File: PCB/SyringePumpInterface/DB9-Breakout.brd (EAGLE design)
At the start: 37.3 x 32.5 mm, 3 parts, among them J2 AUDIO_JACK_3.5MM_PTH

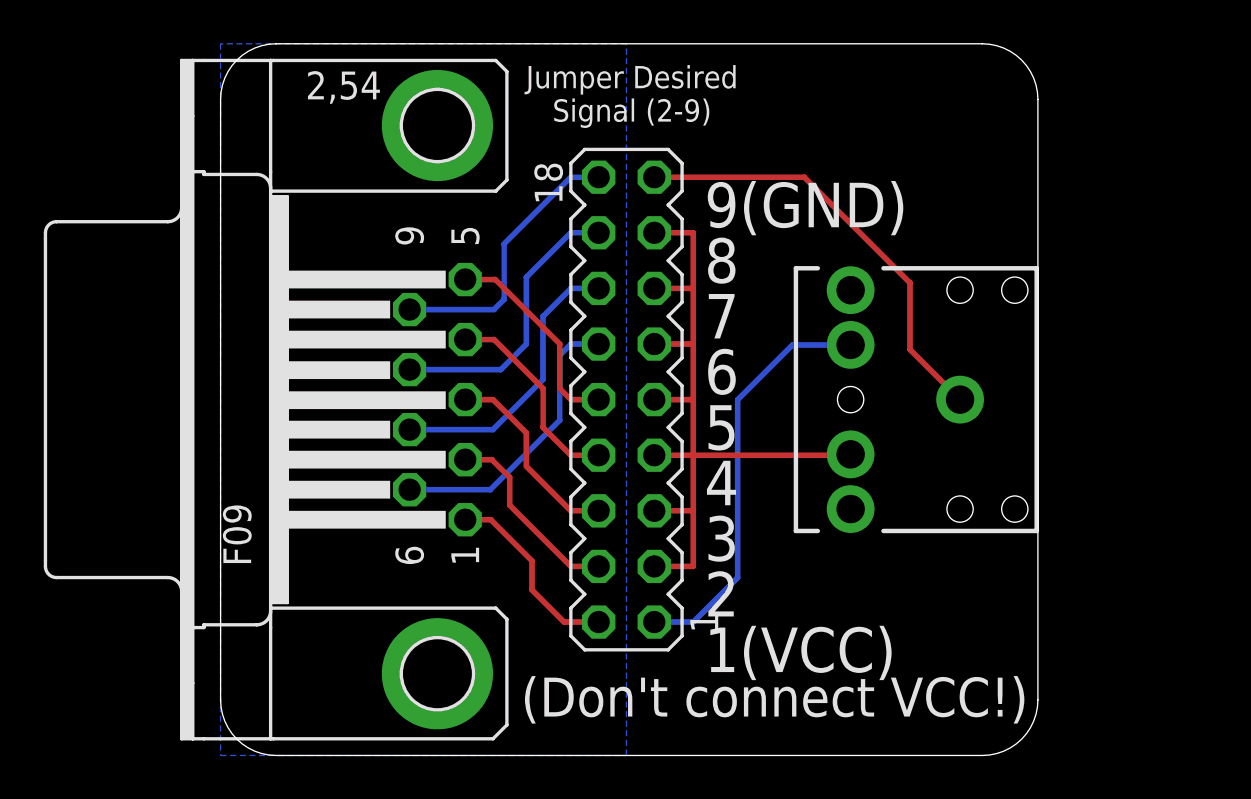
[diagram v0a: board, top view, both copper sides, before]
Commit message: New mouse-scale nose poke foodwell designs added. Also a flexible PCB beam break pcb. Also updated DB9 breakout for the syringe pump that has a jumper to choose the pulse pin.
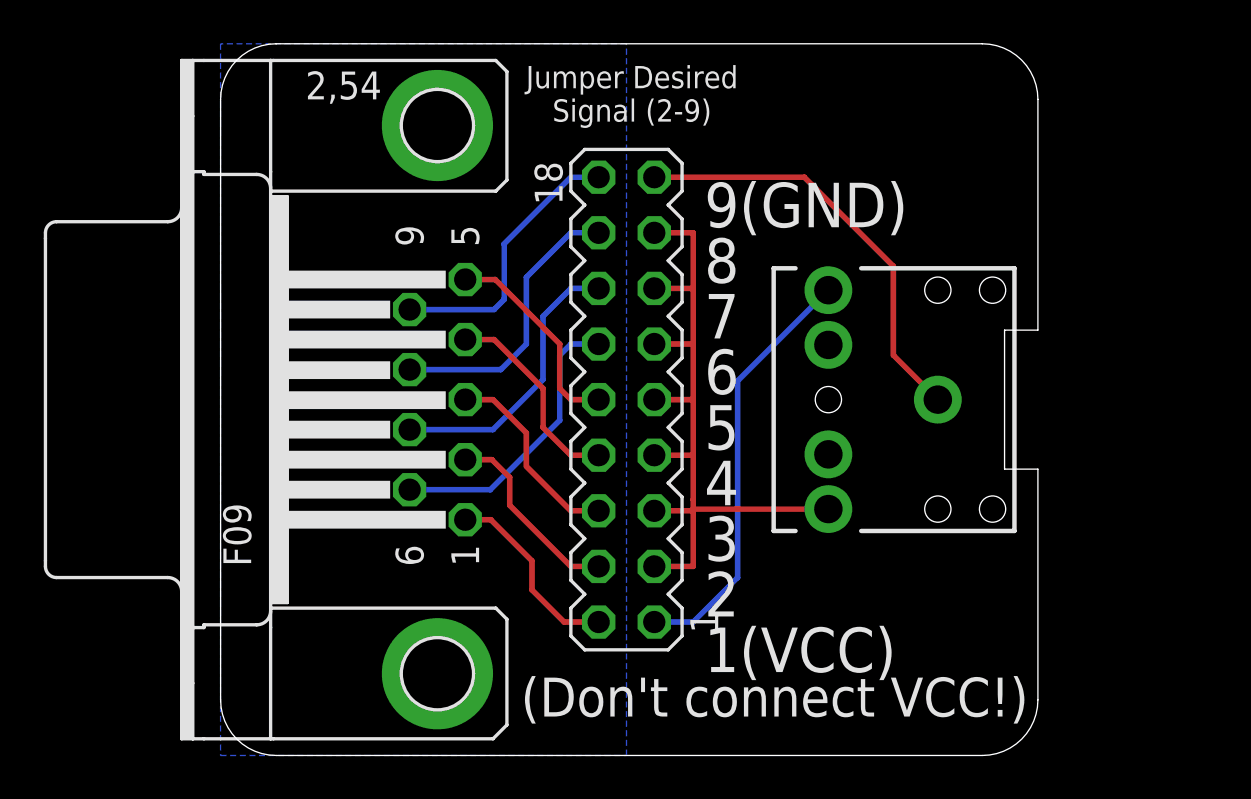
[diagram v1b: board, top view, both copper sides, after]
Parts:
- moved J2 1.02 mm to (32.8, 16.3)
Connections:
- net SIGNAL: now also J2.RING; no longer J2.RSH
- net VCC: now also J2.TIP; no longer J2.TSH
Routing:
- net SIGNAL: track 34.9 -> 33.9 mm
- net VCC: track 19.0 -> 19.5 mm
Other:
- outline, holes or cut-outs redrawn
- board text added: "DB9-Breakout Kemere Lab v 2020.1"
- board text removed: "DB9-Breakout Kemere Lab v 2019.1"
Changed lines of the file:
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@@
 <?xml version="1.0" encoding="utf-8"?>
 <!DOCTYPE eagle SYSTEM "eagle.dtd">
-<eagle version="9.4.2">
+<eagle version="9.5.2">
 <drawing>
 <settings>
@@
 <wire x1="2.54" y1="0" x2="34.798" y2="0" width="0" layer="20"/>
 <wire x1="34.798" y1="0" x2="37.338" y2="2.54" width="0" layer="20" curve="90"/>
-<wire x1="37.338" y1="2.54" x2="37.338" y2="29.972" width="0" layer="20"/>
+<wire x1="37.338" y1="2.54" x2="37.338" y2="13.081" width="0" layer="20"/>
+<wire x1="37.338" y1="13.081" x2="35.814" y2="13.081" width="0" layer="20"/>
+<wire x1="35.814" y1="13.081" x2="35.814" y2="19.431" width="0" layer="20"/>
+<wire x1="35.814" y1="19.431" x2="37.338" y2="19.431" width="0" layer="20"/>
+<wire x1="37.338" y1="19.431" x2="37.338" y2="29.972" width="0" layer="20"/>
 <wire x1="37.338" y1="29.972" x2="34.798" y2="32.512" width="0" layer="20" curve="90"/>
 <text x="22.098" y="26.162" size="2.032" layer="21" font="vector" ratio="16" distance="25" align="top-left">9(GND)
@@
 1(VCC)</text>
 <text x="5.08" y="23.876" size="1.27" layer="22" font="vector" ratio="16" rot="MR270">DB9-Breakout
-Kemere Lab v 2019.1</text>
+Kemere Lab v 2020.1</text>
 <text x="36.068" y="1.016" size="1.27" layer="22" font="vector" ratio="16" rot="MR0">For NE-500 Syringe Pumps
 (http://syringepump.com)</text>
@@
 </autorouter>
 <elements>
-<element name="J2" library="SparkFun-Connectors" library_urn="urn:adsk.eagle:library:513" package="AUDIO-JACK" package3d_urn="urn:adsk.eagle:package:37997/1" value="AUDIO_JACK_3.5MM_PTH" x="33.782" y="16.256" smashed="yes" rot="R180">
-<attribute name="PROD_ID" value="CONN-08774" x="12.192" y="42.926" size="1.778" layer="27" rot="R180" display="off"/>
-<attribute name="SF_ID" value="PRT-08032" x="12.192" y="42.926" size="1.778" layer="27" rot="R180" display="off"/>
+<element name="J2" library="SparkFun-Connectors" library_urn="urn:adsk.eagle:library:513" package="AUDIO-JACK" package3d_urn="urn:adsk.eagle:package:37997/1" value="AUDIO_JACK_3.5MM_PTH" x="32.766" y="16.256" smashed="yes" rot="R180">
+<attribute name="PROD_ID" value="CONN-08774" x="11.176" y="42.926" size="1.778" layer="27" rot="R180" display="off"/>
+<attribute name="SF_ID" value="PRT-08032" x="11.176" y="42.926" size="1.778" layer="27" rot="R180" display="off"/>
 </element>
 <element name="SV1" library="con-lstb-mod" package="MA09-2" package3d_urn="urn:adsk.eagle:package:8362/1" value="" x="18.542" y="16.256" smashed="yes" rot="R90">
@@
 <contactref element="SV1" pad="17"/>
 <wire x1="19.812" y1="26.416" x2="26.67" y2="26.416" width="0.254" layer="1"/>
-<wire x1="31.496" y1="21.59" x2="26.67" y2="26.416" width="0.254" layer="1"/>
-<wire x1="33.782" y1="16.256" x2="31.496" y2="18.542" width="0.254" layer="1"/>
-<wire x1="31.496" y1="18.542" x2="31.496" y2="21.59" width="0.254" layer="1"/>
+<wire x1="30.734" y1="22.352" x2="26.67" y2="26.416" width="0.254" layer="1"/>
+<wire x1="30.734" y1="18.288" x2="32.766" y2="16.256" width="0.254" layer="1"/>
+<wire x1="30.734" y1="22.352" x2="30.734" y2="18.288" width="0.254" layer="1"/>
 </signal>
 <signal name="SIGNAL">
-<contactref element="J2" pad="RSH"/>
 <contactref element="SV1" pad="3"/>
 <contactref element="SV1" pad="5"/>
@@
 <wire x1="21.59" y1="18.796" x2="21.59" y2="16.256" width="0.254" layer="1"/>
 <wire x1="21.59" y1="16.256" x2="21.59" y2="13.716" width="0.254" layer="1"/>
-<wire x1="21.59" y1="13.716" x2="21.59" y2="11.176" width="0.254" layer="1"/>
+<wire x1="21.59" y1="13.716" x2="21.59" y2="11.684" width="0.254" layer="1"/>
+<wire x1="21.59" y1="11.256" x2="21.59" y2="11.176" width="0.254" layer="1"/>
 <wire x1="21.59" y1="11.176" x2="21.59" y2="8.636" width="0.254" layer="1"/>
 <wire x1="21.59" y1="8.636" x2="19.812" y2="8.636" width="0.254" layer="1"/>
-<wire x1="19.812" y1="11.176" x2="21.59" y2="11.176" width="0.254" layer="1"/>
 <wire x1="19.812" y1="13.716" x2="21.59" y2="13.716" width="0.254" layer="1"/>
 <wire x1="19.812" y1="16.256" x2="21.59" y2="16.256" width="0.254" layer="1"/>
 <wire x1="19.812" y1="18.796" x2="21.59" y2="18.796" width="0.254" layer="1"/>
 <wire x1="19.812" y1="21.336" x2="21.59" y2="21.336" width="0.254" layer="1"/>
-<wire x1="28.782" y1="13.756" x2="28.782" y2="13.716" width="0.254" layer="1"/>
-<wire x1="28.782" y1="13.716" x2="21.59" y2="13.716" width="0.254" layer="1"/>
+<contactref element="J2" pad="RING"/>
+<wire x1="19.812" y1="11.176" x2="21.59" y2="11.176" width="0.254" layer="1"/>
+<wire x1="27.766" y1="11.256" x2="21.59" y2="11.256" width="0.254" layer="1"/>
+<wire x1="21.59" y1="11.256" x2="21.59" y2="11.684" width="0.254" layer="1"/>
 </signal>
 <signal name="VCC">
-<contactref element="J2" pad="TSH"/>
 <contactref element="SV1" pad="1"/>
-<wire x1="28.782" y1="18.756" x2="26.122" y2="18.756" width="0.254" layer="16"/>
-<wire x1="23.622" y1="16.256" x2="23.622" y2="8.128" width="0.254" layer="16"/>
-<wire x1="23.622" y1="8.128" x2="21.59" y2="6.096" width="0.254" layer="16"/>
+<wire x1="21.59" y1="6.096" x2="23.622" y2="8.128" width="0.254" layer="16"/>
 <wire x1="21.59" y1="6.096" x2="19.812" y2="6.096" width="0.254" layer="16"/>
-<wire x1="26.122" y1="18.756" x2="23.622" y2="16.256" width="0.254" layer="16"/>
+<contactref element="J2" pad="TIP"/>
+<wire x1="23.622" y1="17.112" x2="27.766" y2="21.256" width="0.254" layer="16"/>
+<wire x1="23.622" y1="8.128" x2="23.622" y2="17.112" width="0.254" layer="16"/>
 </signal>
 </signals>
